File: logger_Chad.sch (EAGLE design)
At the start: 65 parts, among them IC1 LTC4412, J1 POWER_JACKPTH, Q1 FDN360P, Q2 FDN360P, Q3 2N7002PW, Q4 2N7002PW, U1 FT232RL

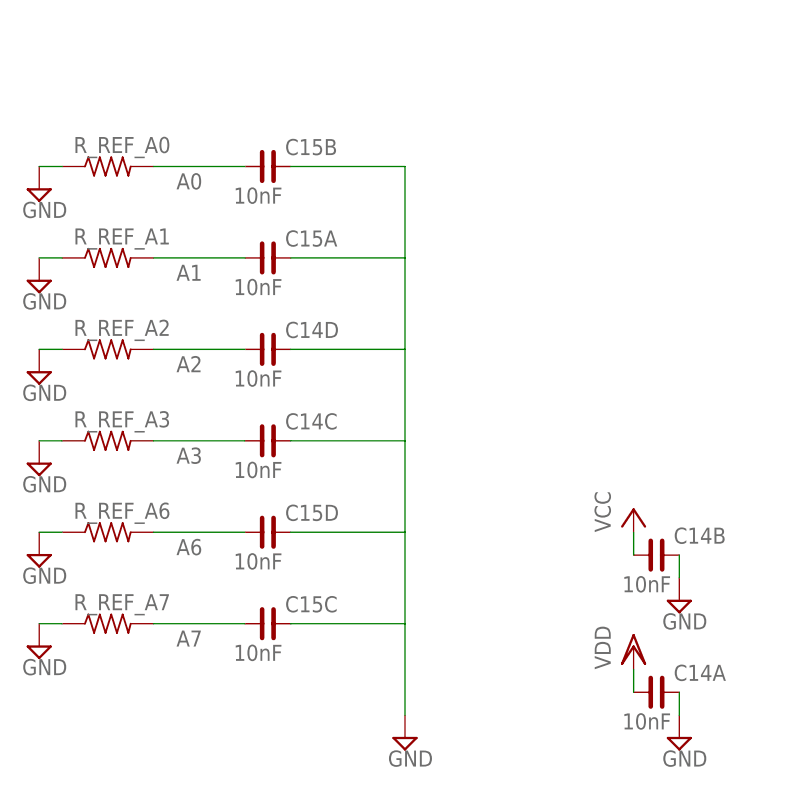
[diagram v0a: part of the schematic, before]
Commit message: Routed board, ground fills and minimized timing device distances
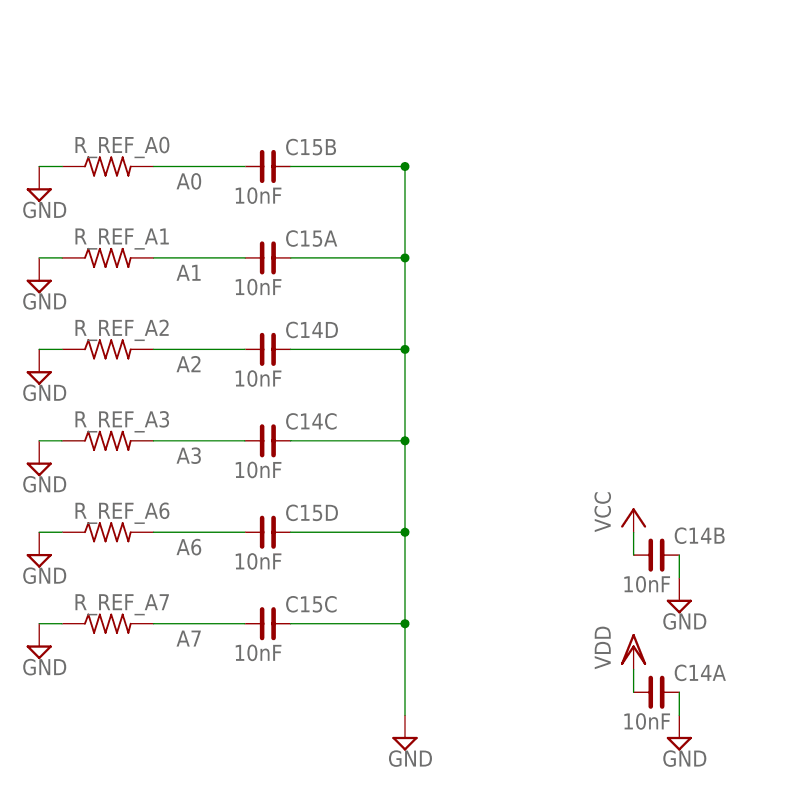
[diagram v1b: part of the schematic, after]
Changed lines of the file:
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@@
 <?xml version="1.0" encoding="utf-8"?>
 <!DOCTYPE eagle SYSTEM "eagle.dtd">
-<eagle version="6.5.0">
+<eagle version="6.6.0">
 <drawing>
 <settings>
@@
 <pinref part="C15" gate="C" pin="2"/>
 <wire x1="254" y1="27.94" x2="266.7" y2="27.94" width="0.1524" layer="91"/>
-</segment>
-<segment>
+<junction x="266.7" y="78.74"/>
+<junction x="266.7" y="68.58"/>
+<junction x="266.7" y="58.42"/>
+<junction x="266.7" y="48.26"/>
+<junction x="266.7" y="38.1"/>
+<junction x="266.7" y="27.94"/>
+</segment>
+<segment>
